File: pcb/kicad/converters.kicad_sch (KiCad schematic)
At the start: 0 parts

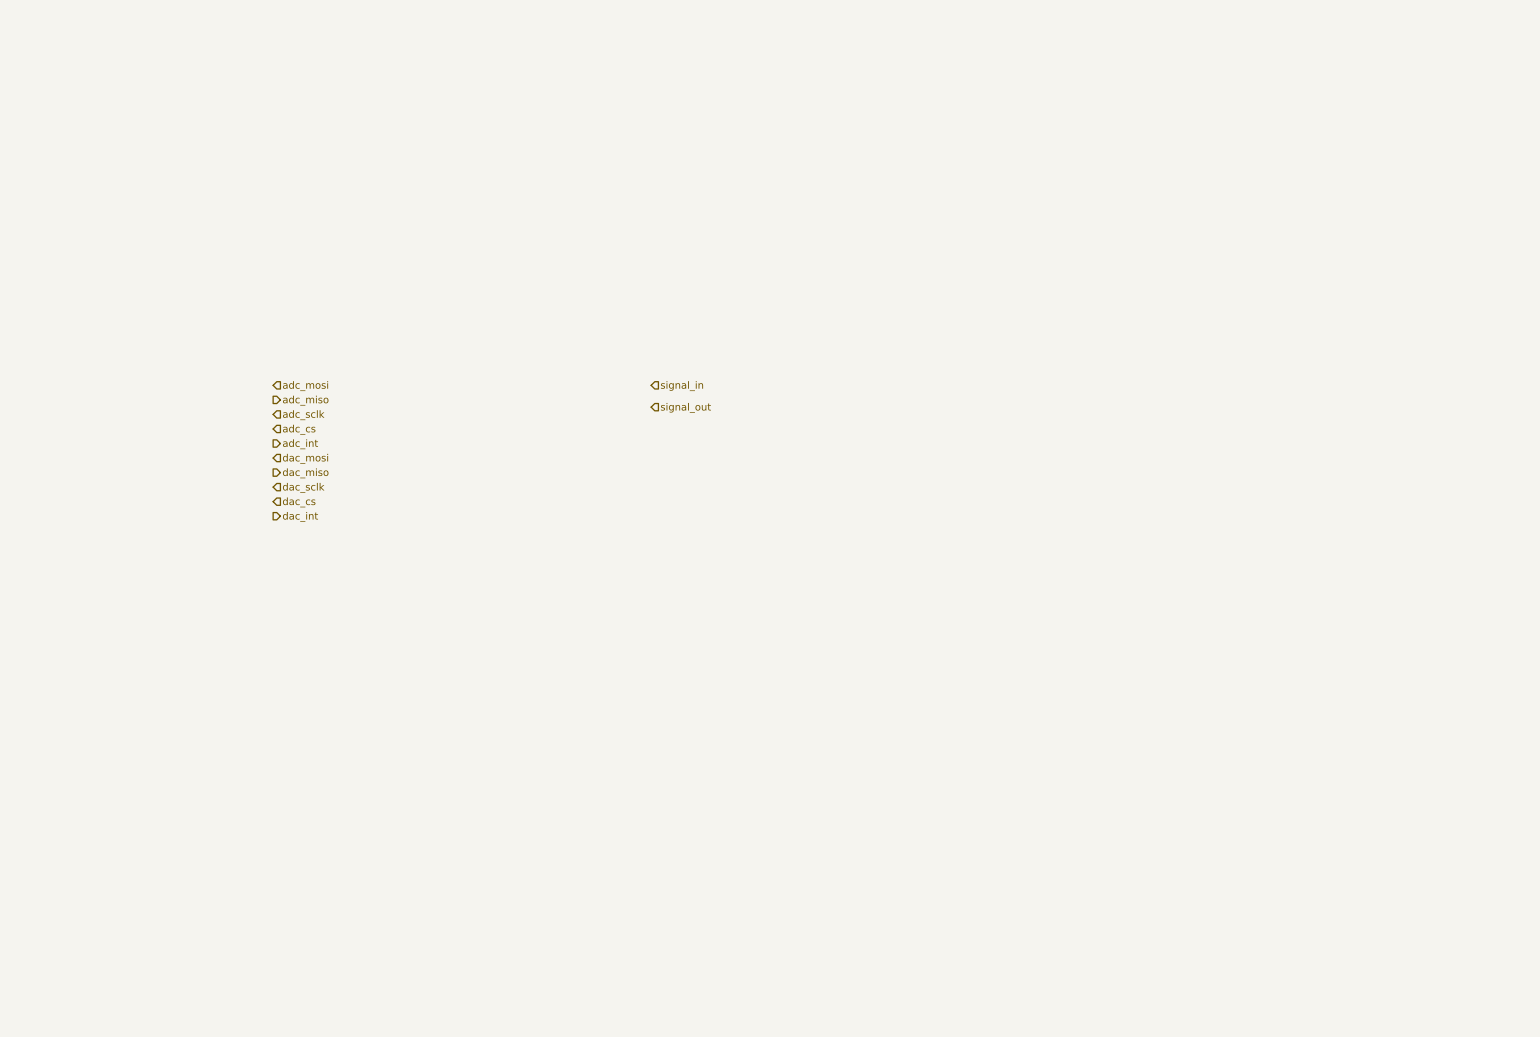
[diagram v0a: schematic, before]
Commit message: Added ADC digital part.
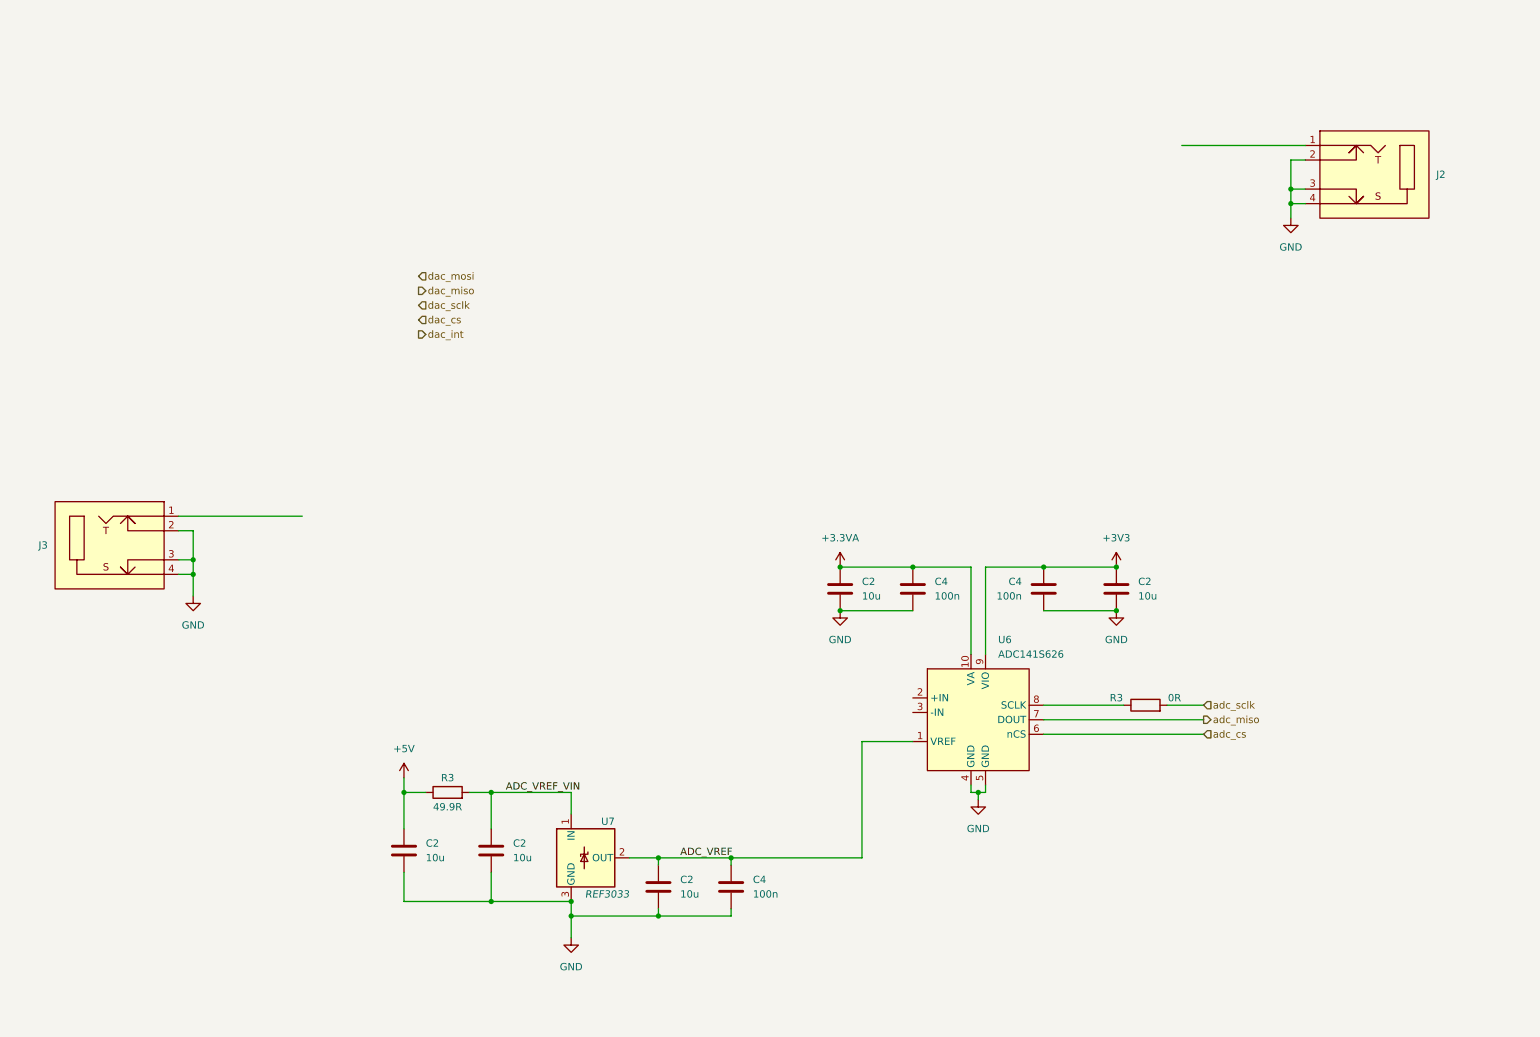
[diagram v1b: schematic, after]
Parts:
- added C2 (x5): 10u, Capacitor_SMD:C_0805_2012Metric, symbol Device:C
- added C4 (x3): 100n, Capacitor_SMD:C_0805_2012Metric, symbol Device:C
- added J2, J3: ~, symbol pedal-components:NMJ4HCD2
- added R3: 49.9R, Resistor_SMD:R_0805_2012Metric, symbol Device:R
- added R3: 0R, Resistor_SMD:R_0805_2012Metric, symbol Device:R
- added U6: ADC141S626, symbol pedal-components:ADC141S626
- added U7: REF3033, Package_TO_SOT_SMD:SOT-23, symbol Reference_Voltage:REF3033
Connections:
- net adc_cs: now also U6.6 (nCS)
- net adc_miso: now also U6.7 (DOUT)
- net adc_sclk: now also R3.2
- new net: R3.1, U6.8 (SCLK)
- new net +3.3VA: C2.1, C4.1, U6.10 (VA)
- new net +3V3: C2.1, C4.1, U6.9 (VIO)
- new net +5V: C2.1, R3.1
- new net ADC_VREF: C2.1, C4.1, U6.1 (VREF), U7.2 (OUT)
- new net ADC_VREF_VIN: C2.1, R3.2, U7.1 (IN)
- new net GND: C2.2, C2.2, C2.2, C2.2, C2.2, C4.2, C4.2, C4.2, J2.2, J2.3, J2.4, J3.2, J3.3, J3.4, U6.4 (GND), U6.5 (GND), U7.3 (GND)

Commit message: Added converters, controls and updated annotations.
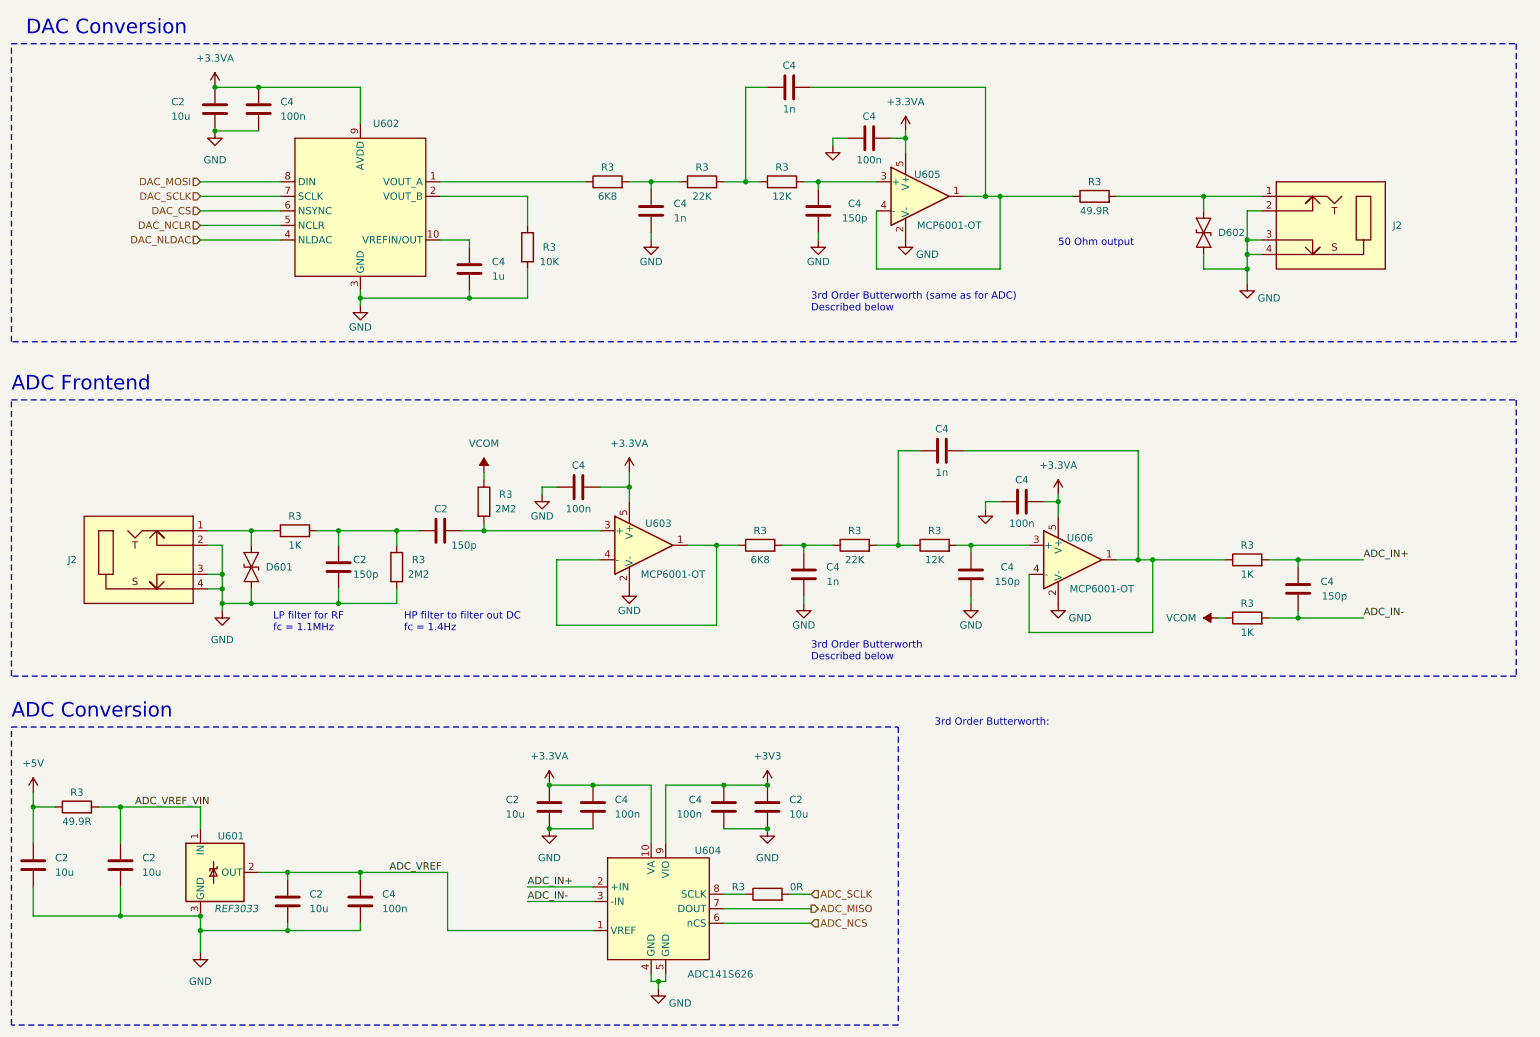
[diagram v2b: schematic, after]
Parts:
- removed J3: ~, symbol pedal-components:NMJ4HCD2
- added C2 (x2), C4 (x3): 150p, Capacitor_SMD:C_0805_2012Metric, symbol Device:C
- added C2: 10u, Capacitor_SMD:C_0805_2012Metric, symbol Device:C
- added C4 (x4): 100n, Capacitor_SMD:C_0805_2012Metric, symbol Device:C
- added C4 (x4): 1n, Capacitor_SMD:C_0805_2012Metric, symbol Device:C
- added C4: 1u, Capacitor_SMD:C_0805_2012Metric, symbol Device:C
- added D601, D602: ~, symbol pedal-components:PESD3V3L1BA
- added J2: ~, symbol pedal-components:NMJ4HCD2
- added R3 (x2): 12K, Resistor_SMD:R_0805_2012Metric, symbol Device:R
- added R3 (x3): 1K, Resistor_SMD:R_0805_2012Metric, symbol Device:R
- added R3: 49.9R, Resistor_SMD:R_0805_2012Metric, symbol Device:R
- added R3: 10K, Resistor_SMD:R_0805_2012Metric, symbol Device:R
- added R3 (x2): 22K, Resistor_SMD:R_0805_2012Metric, symbol Device:R
- added R3 (x2): 2M2, Resistor_SMD:R_0805_2012Metric, symbol Device:R
- added R3 (x2): 6K8, Resistor_SMD:R_0805_2012Metric, symbol Device:R
- added U602: ~, symbol pedal-components:DAC7563SDGSR
- added U603, U605, U606: MCP6001-OT, Package_TO_SOT_SMD:SOT-23-5, symbol Amplifier_Operational:MCP6001-OT
- renumbered U7 to U601, U6 to U604
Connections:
- net +3.3VA: now also C2.1, C4.1, C4.2, C4.2, C4.2, U602.9 (AVDD), U603.5 (V+), U605.5 (V+), U606.5 (V+)
- net GND: now also C2.2, C2.2, C4.1, C4.1, C4.1, C4.1, C4.1, C4.1, C4.1, C4.1, C4.2, D601.1 (A1), D602.1 (A1), J2.2, J2.3, J2.4, R3.1, R3.2, U602.3 (GND), U603.2 (V-), U605.2 (V-), U606.2 (V-)
- net at J2.1: now also D602.2 (A2), R3.2
- net ADC_IN+: now reaches U604.2 (+IN)
- net ADC_IN+: now also C4.2, R3.2
- net ADC_IN-: now reaches U604.3 (-IN)
- net ADC_IN-: now also C4.1, R3.2
- net adc_cs renamed ADC_NCS
- net adc_miso renamed ADC_MISO
- net adc_sclk renamed ADC_SCLK
- new net: C4.2, R3.1, R3.2 (x4)
- new net: C4.2, R3.2, U606.3 (+)
- new net: R3.1, U603.1, U603.4 (-)
- new net: C2.2, R3.2, U603.3 (+)
- new net: C4.2, R3.2, U605.3 (+)
- new net: C4.1, R3.1, U606.1, U606.4 (-)
- new net: C4.1, R3.1, U605.1, U605.4 (-)
- new net: D601.2 (A2), J2.1, R3.1
- new net: C2.1, C2.1, R3.1, R3.2
- new net: R3.2, U602.2 (VOUT_B)
- new net: R3.1, U602.1 (VOUT_A)
- new net: C4.2, U602.10 (VREFIN/OUT)
- new net DAC_CS: U602.6 (NSYNC)
- new net DAC_MOSI: U602.8 (DIN)
- new net DAC_NCLR: U602.5 (NCLR)
- new net DAC_NLDAC: U602.4 (NLDAC)
- new net DAC_SCLK: U602.7 (SCLK)
- new net VCOM: R3.1, R3.1
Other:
- note added: "3rd Order Butterworth (same as for ADC) Described below"
- note added: "3rd Order Butterworth Described below"
- note added: "3rd Order Butterworth:"
- note added: "50 Ohm output"
- note added: "ADC Conversion"
- note added: "ADC Frontend"
- note added: "DAC Conversion"
- note added: "HP filter to filter out DC fc = 1.4Hz"
- note added: "LP filter for RF fc = 1.1MHz"
- moved on the sheet: C2, C4, J2, R3, U601, U604

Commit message: Added PCB layout and fabrication output.
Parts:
- D601, D602: footprint (none) -> pedal-components:PESD3V3L1BA
- J2: value ~ -> NMJ4HCD2; footprint (none) -> pedal-components:NMJ4HCD2
- U602: value ~ -> DAC7563SDGSR; footprint (none) -> pedal-components:10-VSSOP-TI
- U604: footprint (none) -> pedal-components:10-VSSOP-TI
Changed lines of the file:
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@@
     (effects (font (size 1.27 1.27)) (justify left bottom))
   )
-  (text "DAC Conversion" (at 19.05 21.59 0)
+  (text "DAC Conversion" (at 16.51 21.59 0)
     (effects (font (size 2.54 2.54)) (justify left bottom))
   )
@@
       (effects (font (size 1.27 1.27)))
     )
-    (property "Footprint" "" (at 224.79 55.88 0)
+    (property "Footprint" "pedal-components:PESD3V3L1BA" (at 224.79 55.88 0)
       (effects (font (size 1.27 1.27)) hide)
     )
@@
   )
   (symbol (lib_id "pedal-components:NMJ4HCD2") (at 237.49 54.61 0) (unit 1)
-    (in_bom yes) (on_board yes) (dnp no) (fields_autoplaced)
+    (in_bom yes) (on_board yes) (dnp no)
     (property "Reference" "J2" (at 257.81 54.61 0)
       (effects (font (size 1.27 1.27)) (justify left))
     )
-    (property "Value" "~" (at 237.49 54.61 0)
-      (effects (font (size 1.27 1.27)))
-    )
-    (property "Footprint" "" (at 237.49 54.61 0)
+    (property "Value" "NMJ4HCD2" (at 262.89 57.15 0)
+      (effects (font (size 1.27 1.27)))
+    )
+    (property "Footprint" "pedal-components:NMJ4HCD2" (at 237.49 54.61 0)
       (effects (font (size 1.27 1.27)) hide)
     )
@@
       (effects (font (size 1.27 1.27)) (justify left))
     )
-    (property "Footprint" "" (at 128.27 176.53 0)
+    (property "Footprint" "pedal-components:10-VSSOP-TI" (at 128.27 176.53 0)
       (effects (font (size 1.27 1.27)) hide)
     )
@@
       (effects (font (size 1.27 1.27)) (justify left))
     )
-    (property "Value" "~" (at 48.26 113.03 0)
-      (effects (font (size 1.27 1.27)))
-    )
-    (property "Footprint" "" (at 48.26 113.03 0)
+    (property "Value" "NMJ4HCD2" (at 22.86 115.57 0)
+      (effects (font (size 1.27 1.27)))
+    )
+    (property "Footprint" "pedal-components:NMJ4HCD2" (at 48.26 113.03 0)
       (effects (font (size 1.27 1.27)) hide)
     )
@@
       (effects (font (size 1.27 1.27)))
     )
-    (property "Footprint" "" (at 58.42 114.3 0)
+    (property "Footprint" "pedal-components:PESD3V3L1BA" (at 58.42 114.3 0)
       (effects (font (size 1.27 1.27)) hide)
     )
@@
   )
   (symbol (lib_id "pedal-components:DAC7563SDGSR") (at 77.47 50.8 0) (unit 1)
-    (in_bom yes) (on_board yes) (dnp no) (fields_autoplaced)
-    (property "Reference" "U602" (at 79.6641 36.83 0)
-      (effects (font (size 1.27 1.27)) (justify left))
-    )
-    (property "Value" "~" (at 91.44 46.99 0)
-      (effects (font (size 1.27 1.27)))
-    )
-    (property "Footprint" "" (at 91.44 46.99 0)
-      (effects (font (size 1.27 1.27)) hide)
-    )
+    (in_bom yes) (on_board yes) (dnp no)
+    (property "Reference" "U602" (at 78.74 35.56 0)
+      (effects (font (size 1.27 1.27)) (justify left))
+    )
+    (property "Value" "DAC7563SDGSR" (at 86.36 38.1 0)
+      (effects (font (size 1.27 1.27)))
+    )
+    (property "Footprint" "pedal-components:10-VSSOP-TI" (at 91.44 46.99 0)
+      (effects (font (size 1.27 1.27)) hide)
+    )
